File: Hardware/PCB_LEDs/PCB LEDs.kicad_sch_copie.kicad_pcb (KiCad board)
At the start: 2 copper layers, 40.6 x 40.6 mm, 22 parts, among them J1 SCL, J2 SDA, J3 CLOCK, J4 OUTPUT, J5 POWER, U1 PCA9685PW

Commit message: pcb revue
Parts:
- removed J2: SDA, Connector_JST:JST_XH_B2B-XH-A_1x02_P2.50mm_Vertical
- removed J3: CLOCK, Connector_JST:JST_XH_B2B-XH-A_1x02_P2.50mm_Vertical
- removed J4: OUTPUT, Connector_JST:JST_XH_B2B-XH-A_1x02_P2.50mm_Vertical
- removed J5: POWER, Connector_JST:JST_XH_B2B-XH-A_1x02_P2.50mm_Vertical
- D1: value LED_RGBA -> LED_RGB; footprint LED_SMD:LED_RGB_1210 -> LED_SMD:LED_Avago_PLCC6_3x2.8mm
- J1: value SCL -> Conn_01x05; footprint Connector_JST:JST_XH_B2B-XH-A_1x02_P2.50mm_Vertical -> Connector_JST:JST_XH_B5B-XH-A_1x05_P2.50mm_Vertical
- moved D1 14.3 mm to (140.5, 75.4), turned to 180 degrees
- moved J1 12.7 mm to (120.3, 63.0), turned to 0 degrees
- turned R3 to 180 degrees
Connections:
- J1 pad 1: SCL -> GND
- J1 pad 2: GND -> OUTPUT
- U1 pad 25: EXTERNAL_CLOCK -> unconnected-(U1-EXTCLK-Pad25)
- U1 pad 7: unconnected-(U1-LED1-Pad7) -> Net-(D1-GA)
- U1 pad 8: unconnected-(U1-LED2-Pad8) -> Net-(D1-RA)
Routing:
- net GND: track 197.9 -> 14.0 mm
- net unconnected-(U1-EXTCLK-Pad25): track 0.00 -> 16.0 mm, vias 0 -> 2
- net EXTERNAL_CLOCK: track 16.0 -> 0.00 mm, vias 2 -> 0
- net Net-(D4-K): track 4.36 -> 1.77 mm

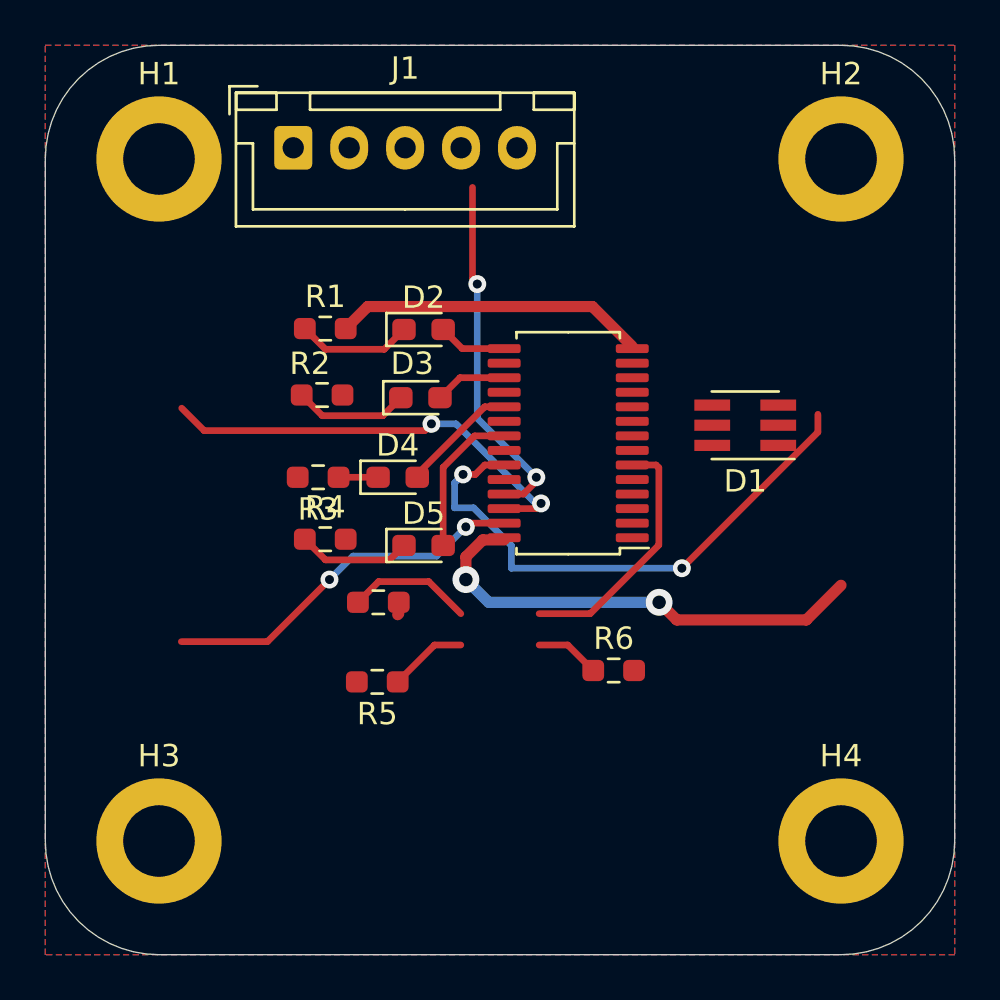
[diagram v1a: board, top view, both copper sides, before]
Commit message: Correction des erreurs après amphi
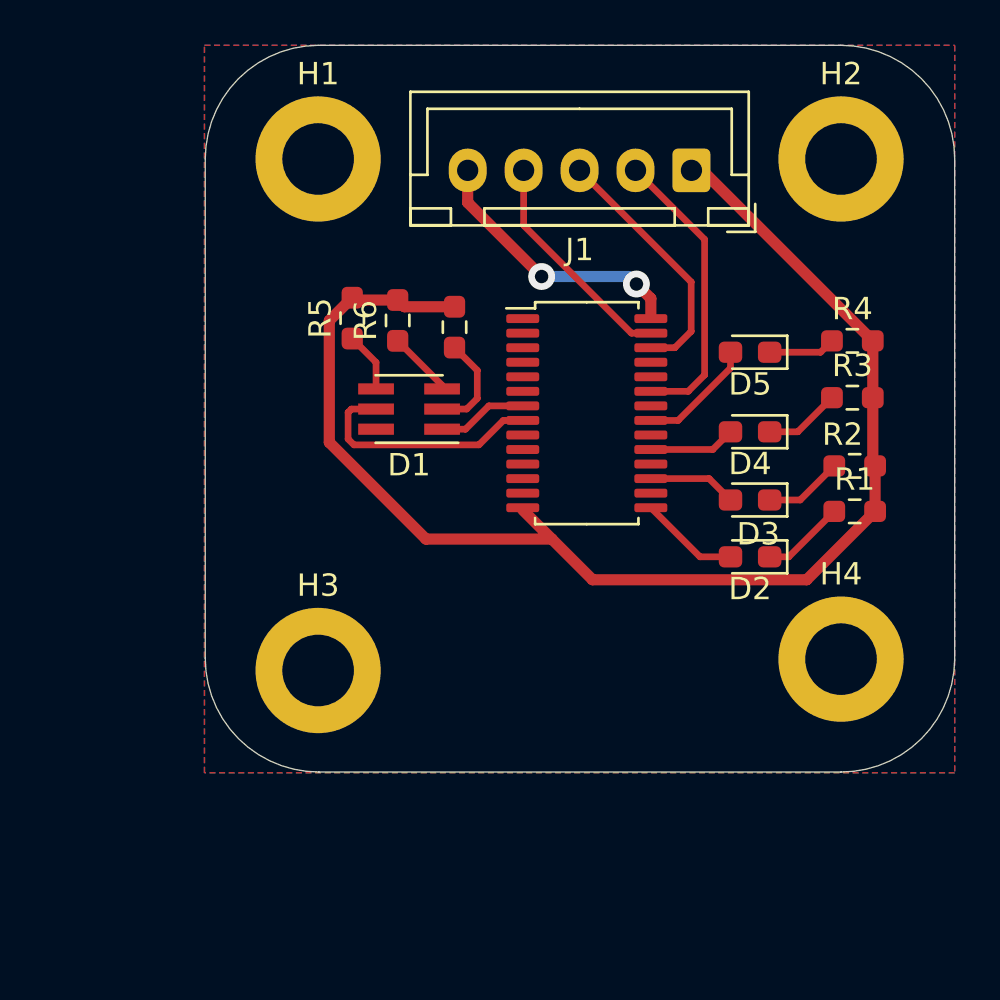
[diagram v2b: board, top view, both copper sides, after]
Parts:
- moved R4 25.2 mm to (145.3, 71.6)
- moved R1 25.0 mm to (145.4, 79.2)
- moved R3 24.1 mm to (145.3, 74.2), turned to 0 degrees
- moved R2 24.0 mm to (145.4, 77.2)
- moved R6 18.4 mm to (125.0, 70.7), turned to 90 degrees
- moved J1 17.8 mm to (138.1, 64.0), turned to 180 degrees
- moved D2 17.8 mm to (140.7, 81.3), turned to 180 degrees
- moved D5 17.0 mm to (140.7, 72.1), turned to 180 degrees
- moved R5 16.3 mm to (122.9, 70.6), turned to 90 degrees
- moved D4 15.9 mm to (140.7, 75.7), turned to 180 degrees
- moved D3 15.4 mm to (140.7, 78.7), turned to 180 degrees
- moved D1 15.0 mm to (125.5, 74.7)
- moved R7 12.8 mm to (127.5, 71.0), turned to 90 degrees
- moved H3 10.4 mm to (121.4, 86.4)
- moved H4 8.13 mm to (144.8, 85.9)
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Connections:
- D1 pad 1: Net-(D1-RK) -> Net-(D1-RA)
- D1 pad 2: Net-(D1-GK) -> Net-(D1-RK)
- D1 pad 4: Net-(D1-BA) -> Net-(D1-GK-Pad4)
- D1 pad 5: Net-(D1-GA) -> Net-(D1-BA)
- D1 pad 6: Net-(D1-RA) -> (no net)
- R5 pad 1: Net-(D1-GK) -> Net-(D1-GK-Pad4)
- U1 pad 6: Net-(D1-BA) -> Net-(U1-LED0)
- U1 pad 7: Net-(D1-GA) -> Net-(D1-RA)
- U1 pad 8: Net-(D1-RA) -> Net-(D1-BA)
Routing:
- net GND: track 14.0 -> 60.6 mm
- net unconnected-(U1-EXTCLK-Pad25): track 16.0 -> 0.00 mm, vias 2 -> 0
- net OUTPUT: track 24.9 -> 13.1 mm, vias 2 -> 0
- net +5V: track 21.2 -> 12.2 mm
- net SCL: track 19.8 -> 11.4 mm, vias 2 -> 0
- net SDA: track 16.6 -> 10.1 mm, vias 2 -> 0
- net Net-(D1-RA): track 0.00 -> 4.04 mm
- net Net-(D1-GK): track 3.50 -> 0.00 mm
- net Net-(D1-GK-Pad4): track 0.00 -> 2.69 mm
- net Net-(D5-K): track 5.08 -> 2.99 mm
- net Net-(D4-K): track 1.77 -> 3.42 mm
- net Net-(D3-K): track 5.15 -> 3.52 mm
- net Net-(D5-A): track 6.80 -> 5.24 mm
- net Net-(D2-K): track 5.18 -> 3.73 mm
- net Net-(D2-A): track 3.08 -> 4.47 mm
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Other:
- board size 40.6 x 40.6 mm -> 33.5 x 32.5 mm

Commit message: Correction erreurs V2
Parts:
- moved D1 2.03 mm to (125.5, 76.7)
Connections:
- D1 pad 3: Net-(D1-6) -> Net-(U1-LED0)
- D1 pad 6: (no net) -> Net-(D1-Pad6)
- R6 pad 1: Net-(D1-6) -> Net-(D1-Pad6)
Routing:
- net Net-(D1-Pad6): track 0.00 -> 8.54 mm, vias 0 -> 2
- net Net-(U1-LED0): track 0.00 -> 4.40 mm
- net Net-(D1-6): track 2.97 -> 0.00 mm
- net Net-(D1-RK): track 4.46 -> 6.88 mm
- net Net-(D1-GK-Pad4): track 2.69 -> 4.90 mm
- net Net-(D1-RA): track 4.04 -> 6.05 mm
- net GND: track 60.6 -> 62.1 mm
- net Net-(D1-BA): track 10.9 -> 10.2 mm
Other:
- board text added: "B"
- board text added: "Cohoma"
- board text added: "Led driver"
- board text added: "T"
